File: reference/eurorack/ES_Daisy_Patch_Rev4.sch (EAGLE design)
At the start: 215 parts, among them Q1 MMBT3904, Q2 MMBT3904, U11 TL074, U13 TL074, U14 TL074, U15 OPTOISOLATOR_H11L1M, U16 TL074, U2 AK4556, U3 MICRO_SD_CARDCENTERED, U4 TL074, U5 TL074, U6 LM4040-10V, U7 MCP6004

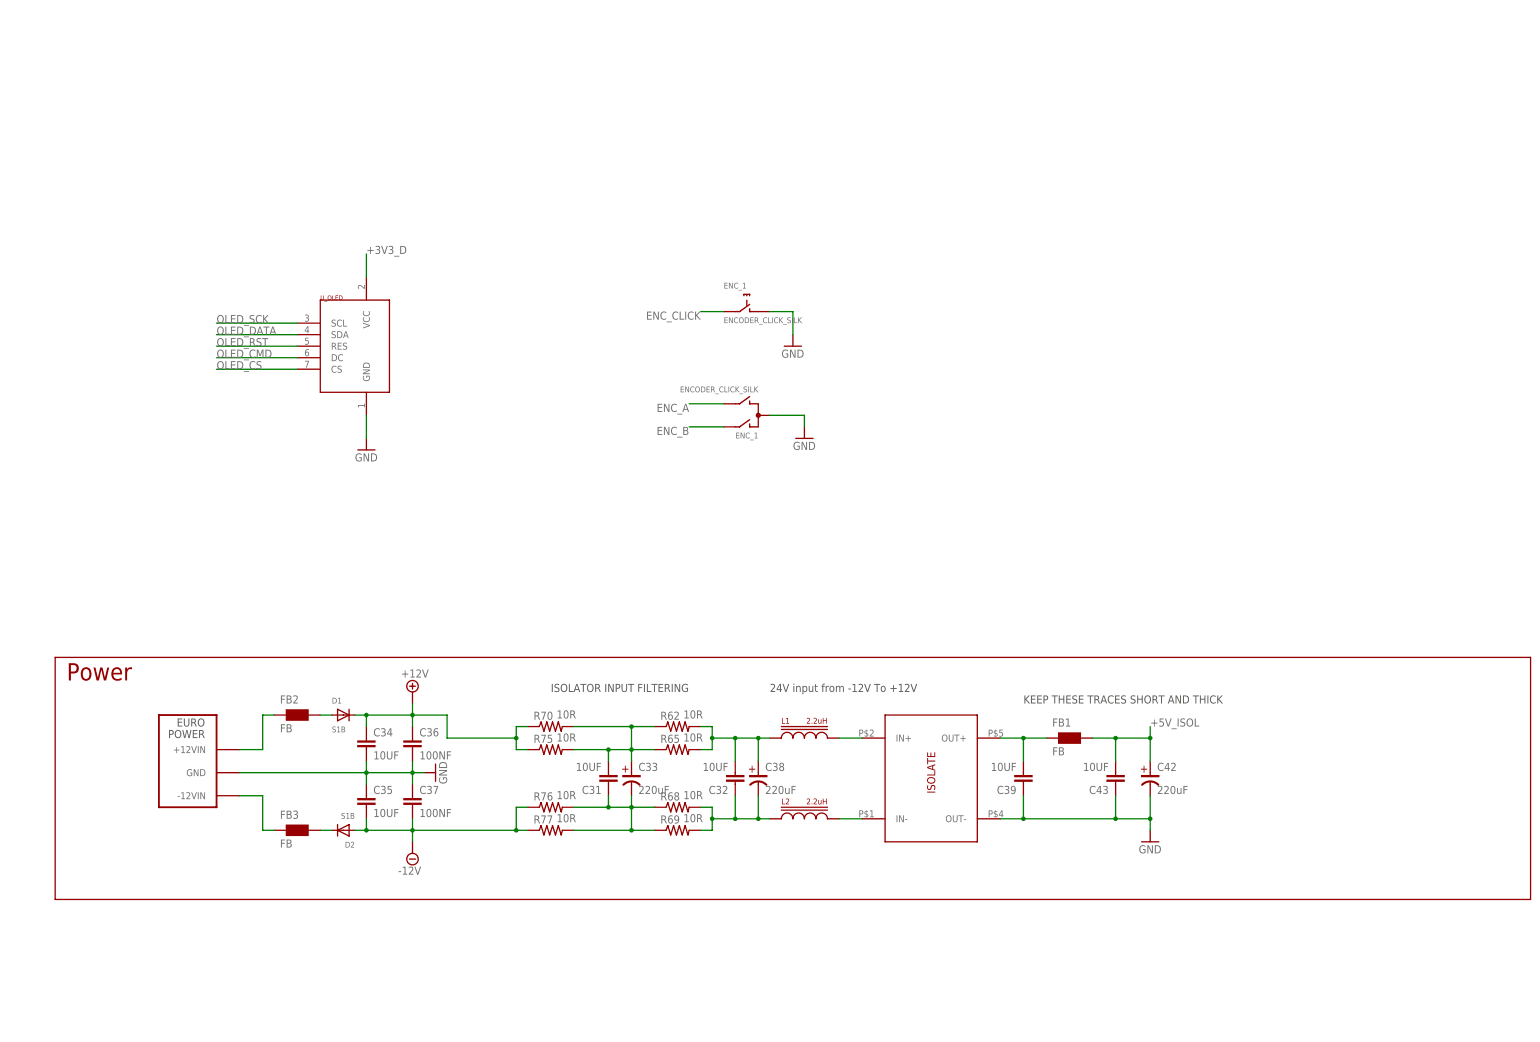
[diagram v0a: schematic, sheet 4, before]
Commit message: updated Patch sch
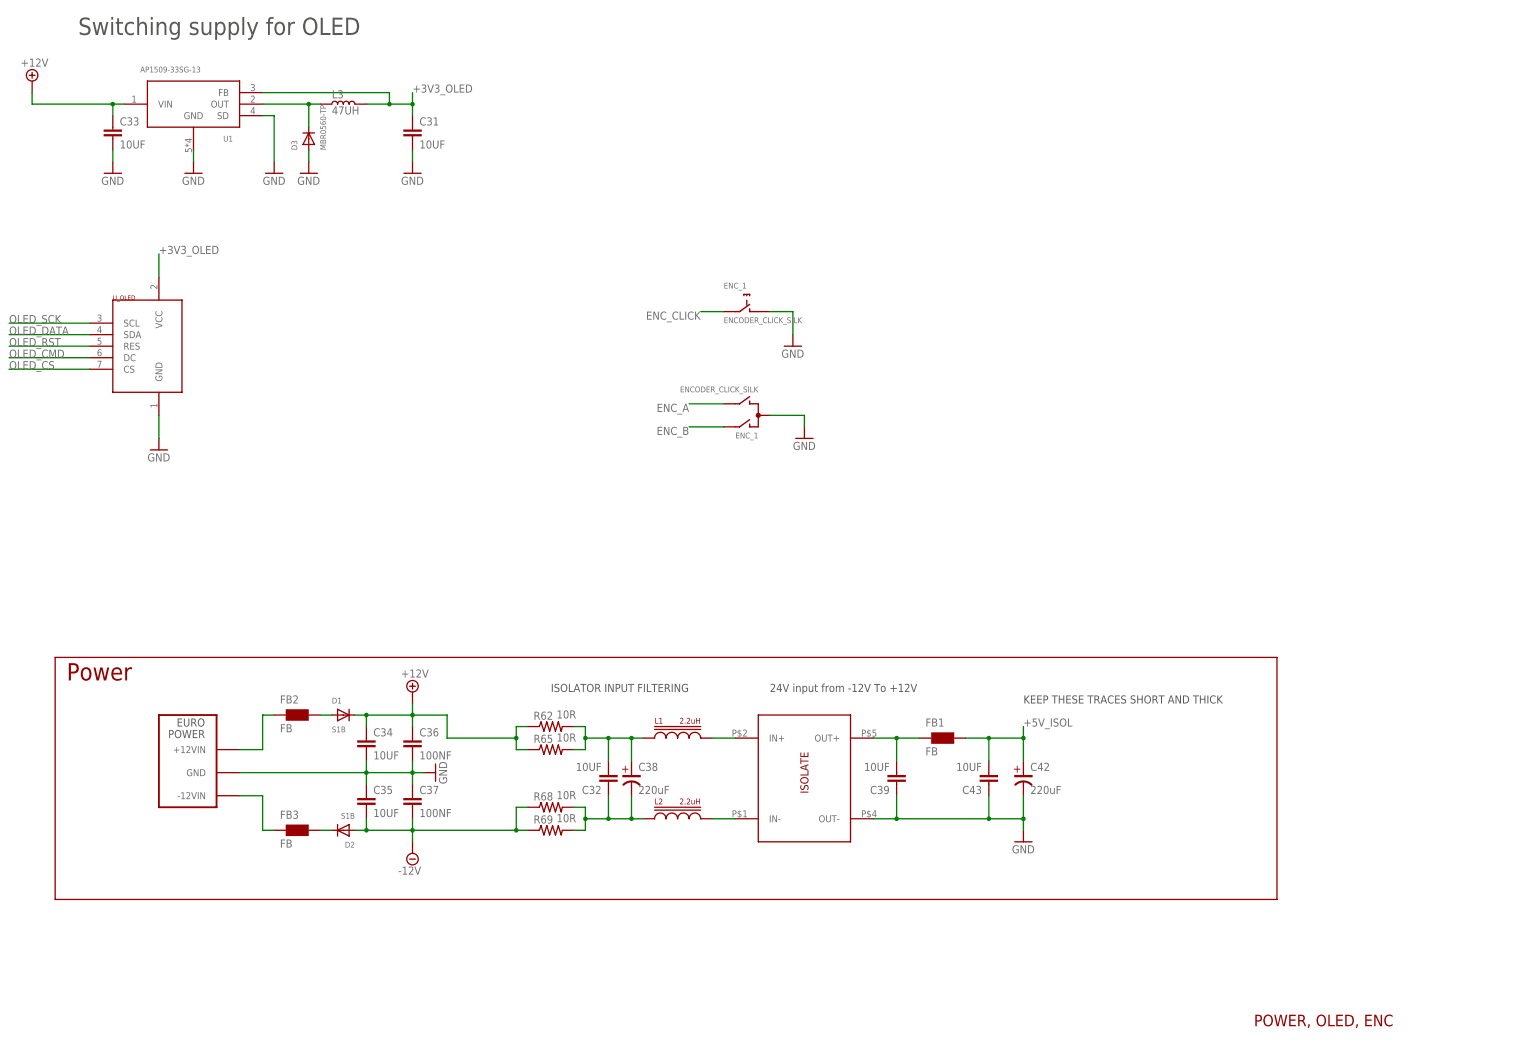
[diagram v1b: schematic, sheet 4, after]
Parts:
- removed R70, R75, R76, R77: 10R, Electrosmith-Passives:R-US_R0603
- added D3: MBR0560-TP, ElectroSmith:DIODESOD-123
- added L3: 47UH, ElectroSmith:SRN3015TA
- added U1: AP1509-33SG-13, Electrosmith-Power:AP1509-3V3
- C31: device Electrosmith-Passives:C-EUC0805 -> ElectroSmith:C-EUC0805
- C33: value 220uF -> 10UF; device Electrosmith-Passives:C-EU-POL_D -> ElectroSmith:C-EUC0805
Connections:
- removed net N$49: C31.2, C33.POS, R62.1, R65.1, R70.2, R75.2
- removed net N$50: C31.1, C33.NEG, R68.1, R69.1, R76.2, R77.2
- new net +3V3_OLED: C31.1, L3.P$2, U1.FB, U_OLED.VCC
- new net N$76: D3.C, L3.P$1, U1.OUT
- net +12V: now also C33.1, R62.1, R65.1, U1.VIN; no longer R70.1, R75.1
- net +3V3_D: no longer U_OLED.VCC
- net -12V: now also R68.1, R69.1; no longer R76.1, R77.1
- net GND: now also C31.2, C33.2, D3.A, U1.GND, U1.SD
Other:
- note added: "DNI Resistors for backwards MIDI connectors"
- note added: "Daisy / MIDI / SAI / SDMMC"
- note added: "IN: -5V to +5V CV summed with POT OUT: +3V3 to 0V"
- note added: "POWER, OLED, ENC"
- note added: "Switching supply for OLED"
- note removed: "Daisy / MIDI / SAI"
- note removed: "IN: -5V to 5V CV summed with POT OUT: 3.3V to 0V"
- moved on the sheet: C31, C32, C38, C39, C42, C43, FB1, L1, L2, R62, R65, R68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
